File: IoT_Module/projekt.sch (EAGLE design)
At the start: 20 parts, among them IC1 ESP12E_DEVKIT, IC2 LF50CP, IC3 LEVEL_SHIFTER, IC4 LEVEL_SHIFTER, J1 PSH02-02W

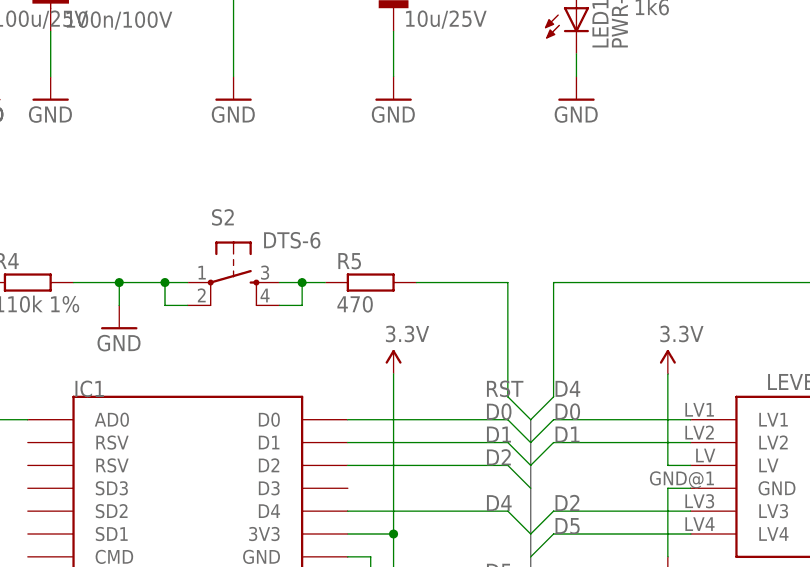
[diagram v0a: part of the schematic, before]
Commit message: Added door sensor
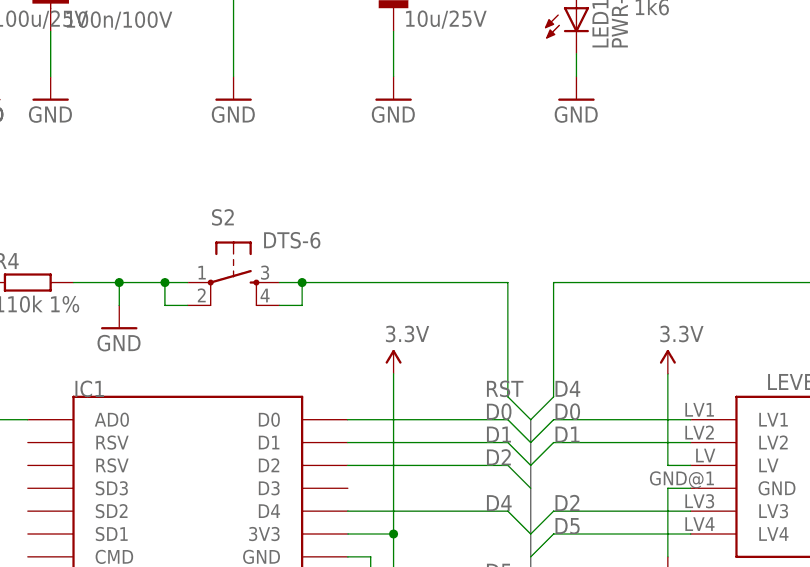
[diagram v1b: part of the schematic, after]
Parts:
- removed R5: 470, rcl:R-EU_R1206
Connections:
- removed net N$4: R5.1, S2.3, S2.4
- net RST: now also S2.3, S2.4; no longer R5.2
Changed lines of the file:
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@@
 <part name="FRAME1" library="SparkFun-Aesthetics" deviceset="FRAME-A4L" device="">
 <attribute name="CNAME" value="IoT Lab Module"/>
-<attribute name="CREVISION" value="1"/>
+<attribute name="CREVISION" value="2"/>
 <attribute name="DESIGNER" value="Vagovszky M."/>
 </part>
@@
 <part name="IC3" library="level_shifter" deviceset="LEVEL_SHIFTER" device=""/>
 <part name="S2" library="switch-tact" deviceset="DTS-6" device=""/>
-<part name="R5" library="rcl" deviceset="R-EU_" device="R1206" value="470"/>
 <part name="GND13" library="supply1" deviceset="GND" device=""/>
 <part name="IC4" library="level_shifter" deviceset="LEVEL_SHIFTER" device=""/>
@@
 <instance part="IC3" gate="G$1" x="124.46" y="91.44" rot="R180"/>
 <instance part="S2" gate="G$1" x="58.42" y="111.76" rot="R270"/>
-<instance part="R5" gate="G$1" x="73.66" y="111.76"/>
 <instance part="GND13" gate="1" x="25.4" y="132.08"/>
 <instance part="IC4" gate="G$1" x="124.46" y="55.88" rot="R180"/>
@@
 </segment>
 </net>
-<net name="N$4" class="0">
-<segment>
-<pinref part="S2" gate="G$1" pin="3"/>
-<pinref part="R5" gate="G$1" pin="1"/>
-<wire x1="63.5" y1="111.76" x2="66.04" y2="111.76" width="0.1524" layer="91"/>
-<pinref part="S2" gate="G$1" pin="4"/>
-<wire x1="66.04" y1="111.76" x2="68.58" y2="111.76" width="0.1524" layer="91"/>
-<wire x1="63.5" y1="109.22" x2="66.04" y2="109.22" width="0.1524" layer="91"/>
-<wire x1="66.04" y1="109.22" x2="66.04" y2="111.76" width="0.1524" layer="91"/>
-<junction x="66.04" y="111.76"/>
-</segment>
-</net>
 <net name="3.3V" class="0">
 <segment>
@@
 </segment>
 <segment>
-<pinref part="R5" gate="G$1" pin="2"/>
-<wire x1="78.74" y1="111.76" x2="88.9" y2="111.76" width="0.1524" layer="91"/>
 <wire x1="88.9" y1="111.76" x2="88.9" y2="99.06" width="0.1524" layer="91"/>
 <wire x1="88.9" y1="99.06" x2="91.44" y2="96.52" width="0.1524" layer="91"/>
 <label x="86.36" y="99.06" size="1.778" layer="95"/>
-</segment>
-<segment>
+<pinref part="S2" gate="G$1" pin="3"/>
+<wire x1="63.5" y1="111.76" x2="66.04" y2="111.76" width="0.1524" layer="91"/>
+<pinref part="S2" gate="G$1" pin="4"/>
+<wire x1="63.5" y1="109.22" x2="66.04" y2="109.22" width="0.1524" layer="91"/>
+<wire x1="66.04" y1="109.22" x2="66.04" y2="111.76" width="0.1524" layer="91"/>
+<junction x="66.04" y="111.76"/>
+<wire x1="88.9" y1="111.76" x2="66.04" y2="111.76" width="0.1524" layer="91"/>
+</segment>
+<segment>
